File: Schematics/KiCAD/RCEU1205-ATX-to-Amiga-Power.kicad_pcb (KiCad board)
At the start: 2 copper layers, 62 x 44.5 mm, 11 parts, among them J1 ATX-24, J10 Conn_01x02, J11 Conn_01x02, J2 Conn_01x02, J3 Conn_01x05, J4 Conn_01x04, J5 Conn_01x04, J6 Conn_01x02, J7 Conn_01x02, J8 Conn_01x02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

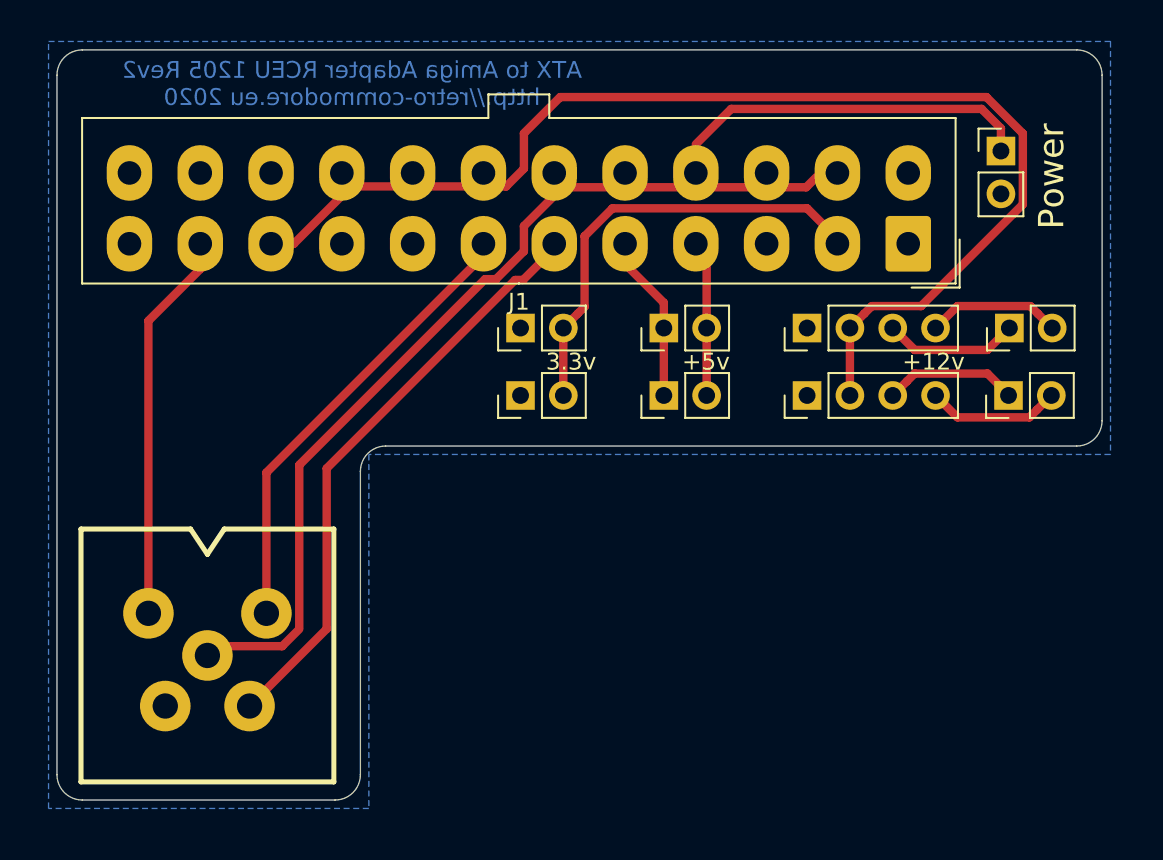
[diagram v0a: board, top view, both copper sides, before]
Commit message: Fixing connector to be seated on the correct side + expanded holes for atx connector.
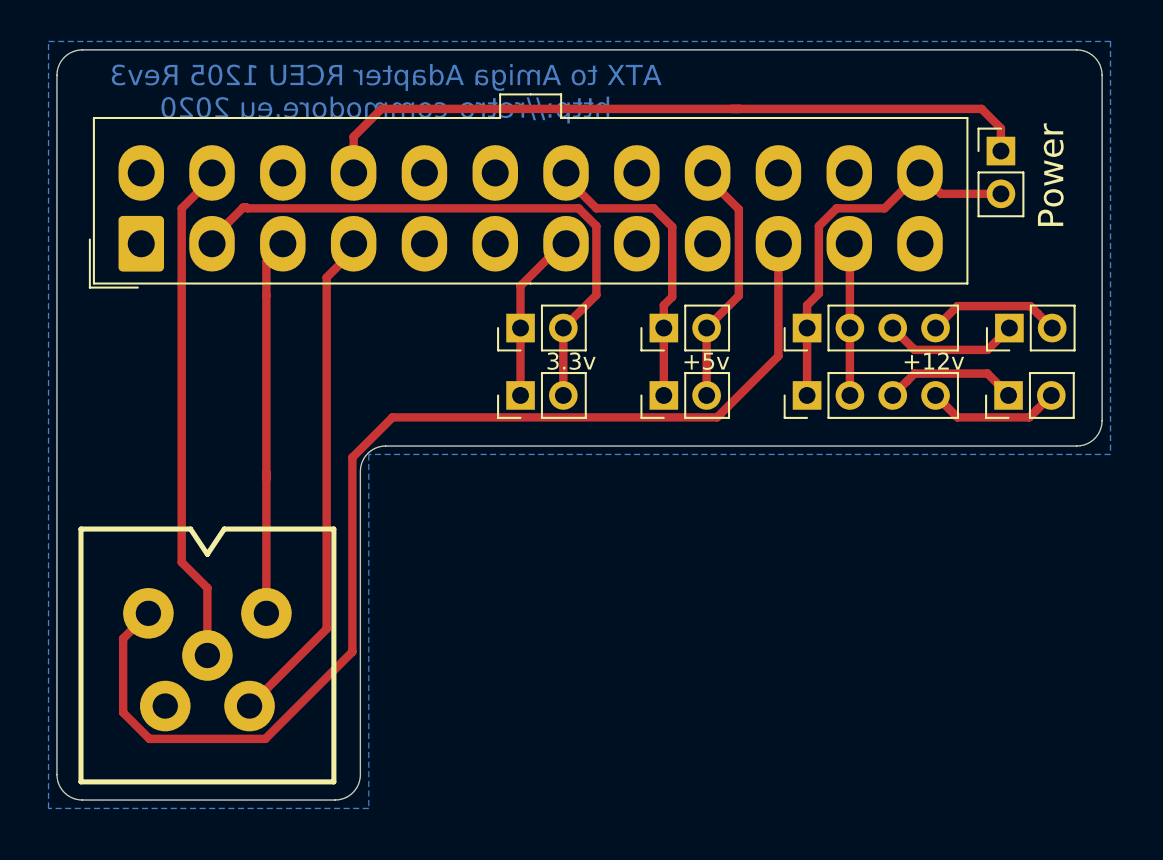
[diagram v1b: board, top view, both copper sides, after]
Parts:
- J1: moved to B.Cu
- moved J1 45.5 mm to (109.0, 78.5), turned to 0 degrees
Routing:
- net GNDREF: track 37.2 -> 73.9 mm
- net /-12v: track 56.4 -> 30.8 mm
- net /PWRON: track 21.2 -> 43.6 mm
- net /+12v: track 95.0 -> 77.9 mm
- net /+3.3v: track 26.7 -> 35.2 mm
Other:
- board text added: "ATX to Amiga Adapter RCEU 1205 Rev3 http://retro-commodore.eu 2020"
- board text removed: "ATX to Amiga Adapter RCEU 1205 Rev2 http://retro-commodore.eu 2020"

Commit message: Fixing som cosmetics
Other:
- board text added: "12v"
- board text added: "5v"
- board text added: "Power on"
- board text removed: "+12v"
- board text removed: "+5v"
- board text removed: "Power"
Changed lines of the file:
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@@
       (net 5 GNDREF))
   )
-  (gr_text +12v (at 156 85.5) (layer F.SilkS)
+  (gr_text 12v (at 151 85.5) (layer F.SilkS)
     (effects (font (size 1 1) (thickness 0.2)))
   )
-  (gr_text Power (at 163 74.5 90) (layer F.SilkS)
+  (gr_text "Power on" (at 163 74.5 90) (layer F.SilkS)
     (effects (font (size 1.5 1.5) (thickness 0.3)))
   )
-  (gr_text +5v (at 142.5 85.5) (layer F.SilkS)
+  (gr_text 5v (at 142.5 85.5) (layer F.SilkS)
     (effects (font (size 1 1) (thickness 0.15)))
   )

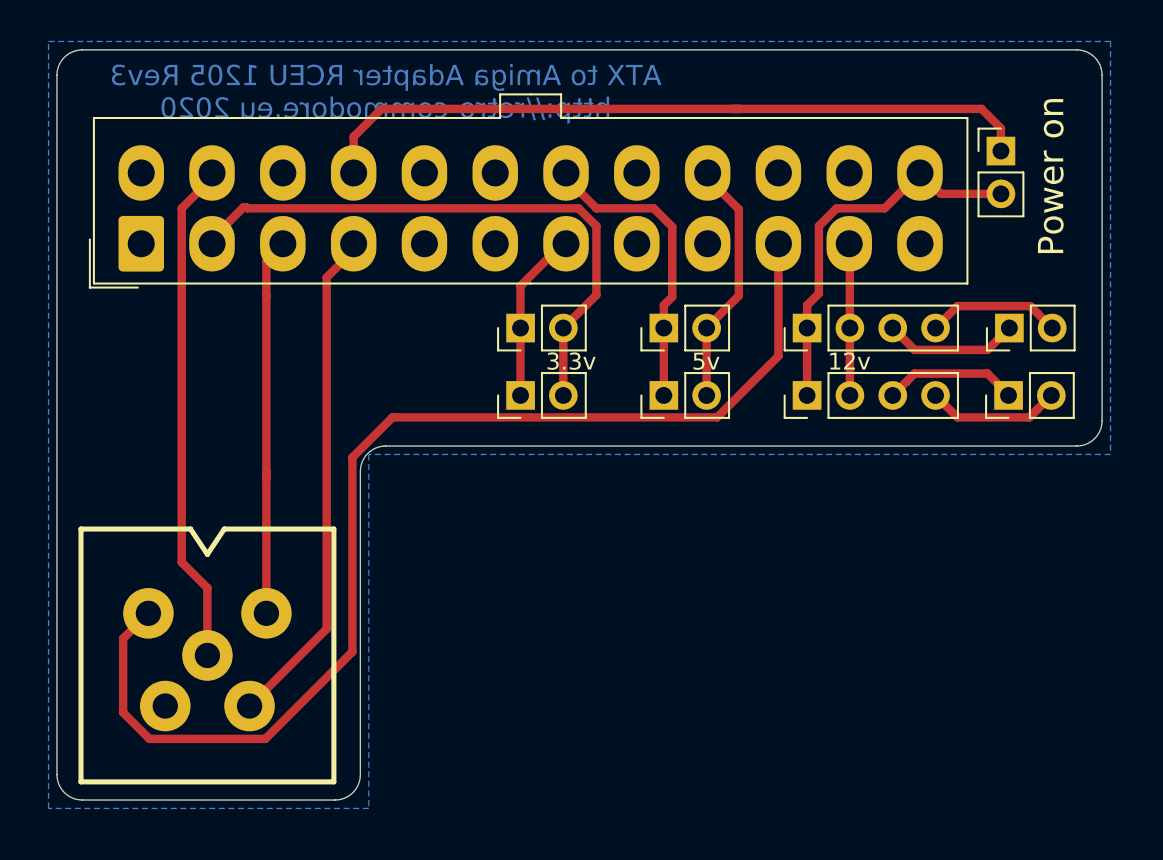
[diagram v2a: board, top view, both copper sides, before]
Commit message: Fixed ATX connector, rechecked pinout
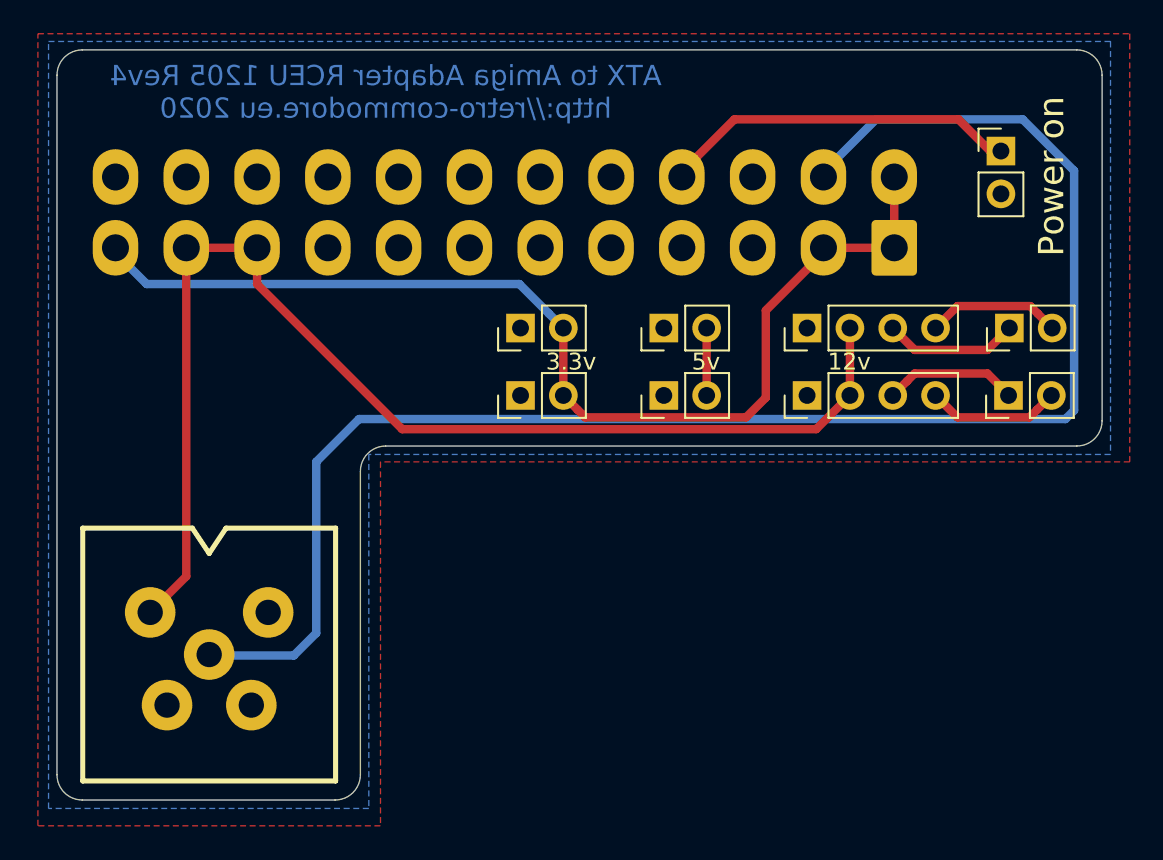
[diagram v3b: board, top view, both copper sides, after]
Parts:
- J1: moved to F.Cu
- moved J1 44.7 mm to (153.7, 78.7), turned to 180 degrees
- moved J3 0.12 mm to (113.0, 102.9)
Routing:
- net GNDREF: track 73.9 -> 0.00 mm
- net /-12v: track 30.8 -> 95.3 mm
- net /+5v: track 44.7 -> 4.00 mm
- net /+3.3v: track 35.2 -> 64.5 mm
- net /PWRON: track 43.6 -> 21.3 mm
- net /+12v: track 77.9 -> 72.7 mm
- added copper zone on F.Cu, net /+5v
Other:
- board text added: "ATX to Amiga Adapter RCEU 1205 Rev4 http://retro-commodore.eu 2020"
- board text removed: "ATX to Amiga Adapter RCEU 1205 Rev3 http://retro-commodore.eu 2020"
